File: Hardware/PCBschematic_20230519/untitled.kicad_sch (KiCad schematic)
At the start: 24 parts, among them J3 Conn_01x02, Q1 SQ2310ES, U3 NCS210

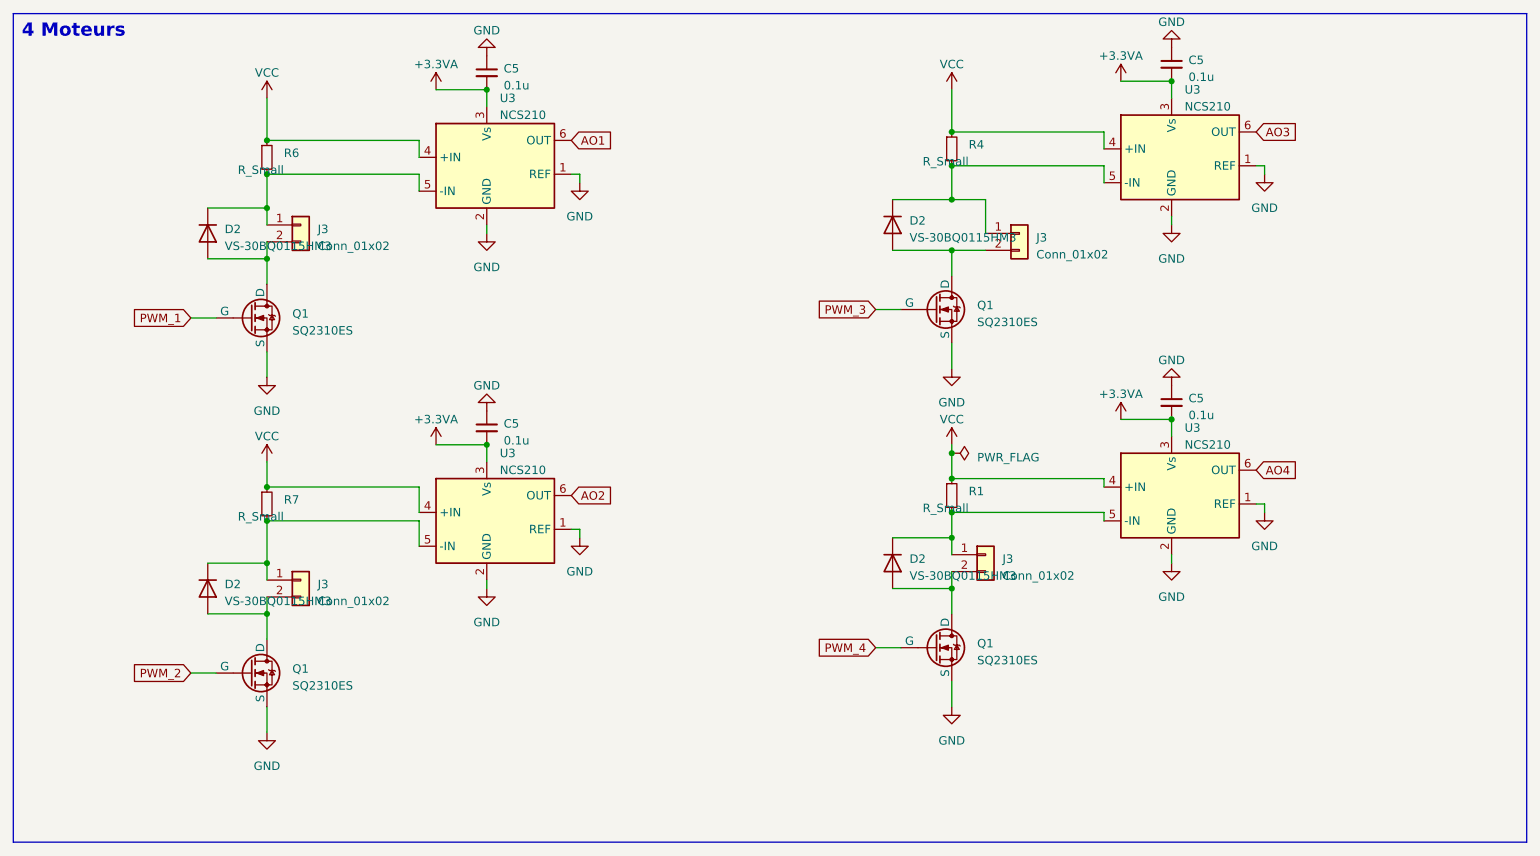
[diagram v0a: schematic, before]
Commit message: ajout description composants sur schématique
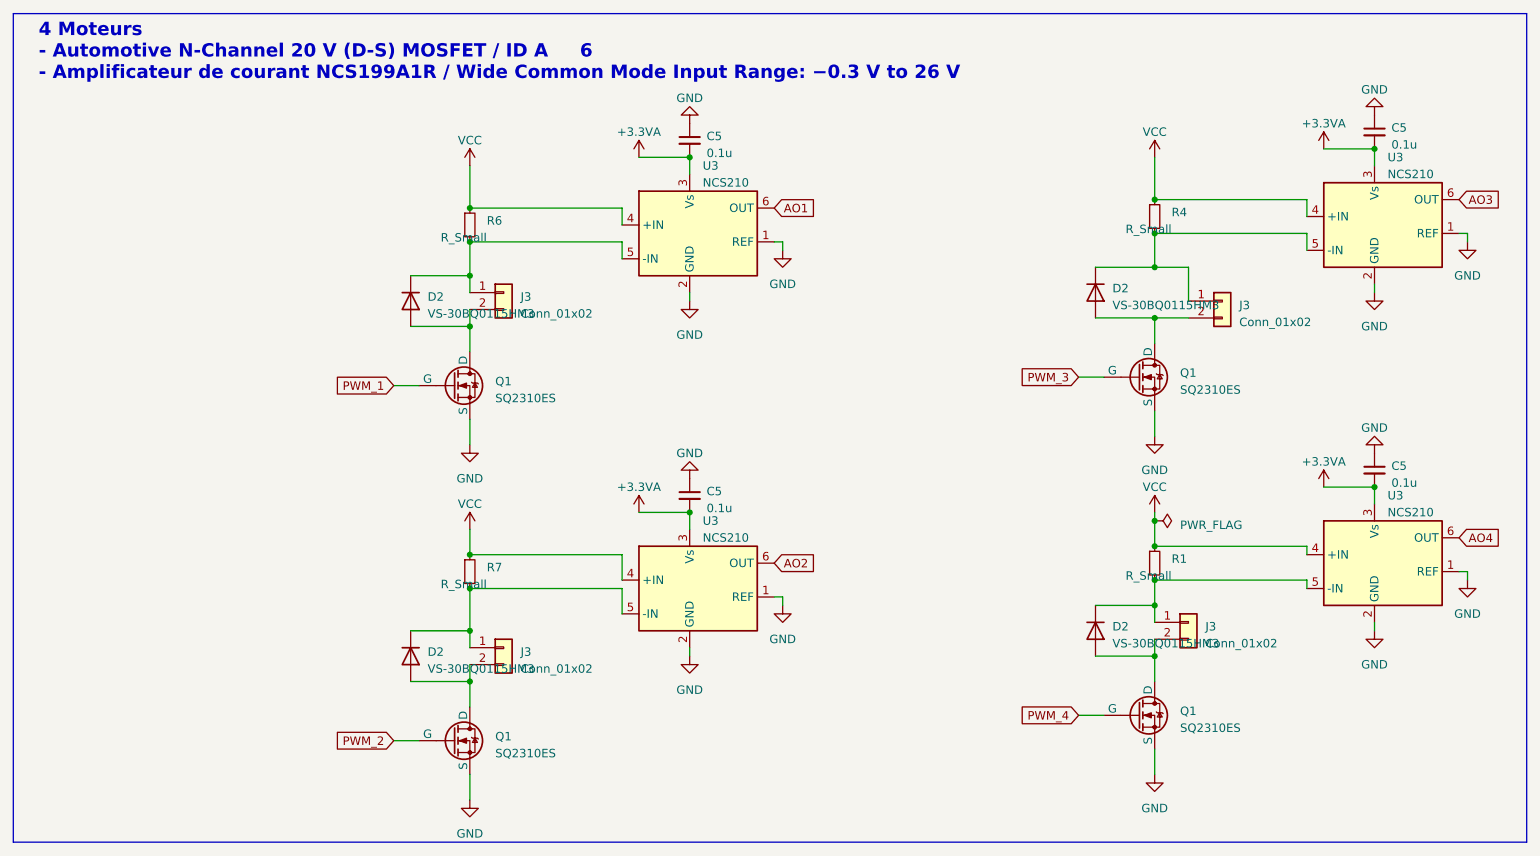
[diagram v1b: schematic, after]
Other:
- note added: "4 Moteurs - Automotive N-Channel 20 V (D-S) MOSFET / ID A 6 - Amplificateur de courant NCS199A1R / Wide Common Mode Input Range: −0.3 V to 26 V"
- note removed: "4 Moteurs"
- moved on the sheet: C5, D2, J3, Q1, R1, R4, R6, R7, U3
